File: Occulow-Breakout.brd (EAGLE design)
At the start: 49.5 x 50.8 mm, 18 parts

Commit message: Rearrangements and labeling
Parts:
- moved SL2 10.8 mm to (45.7, 23.2), turned to 270 degrees
- moved C1 3.81 mm to (47.5, 12.1)
- moved C2 3.81 mm to (44.3, 7.30)
- moved C3 3.81 mm to (43.8, 12.1)
- moved R4 3.81 mm to (45.9, 3.65)
- moved U$2 1.66 mm to (34.9, 14.4)
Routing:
- net GR_INT: track 25.1 -> 39.1 mm
- net GR_VCC: track 56.0 -> 43.7 mm
- net GR_SCL: track 26.5 -> 37.5 mm
- net GR_SDA: track 29.0 -> 38.8 mm
- net GR_GND: track 57.4 -> 48.1 mm
- net N$2: track 6.96 -> 9.66 mm
- net N$4: track 5.38 -> 6.77 mm
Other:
- board text added: "Grid-EYE Breakout"
- board text added: "INT"
- board text added: "PIR Breakout"
- board text added: "SCL"
- board text added: "SDA"

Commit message: Rename caps, bom
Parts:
- renumbered C10 to C4, C11 to C5
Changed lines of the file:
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@@
 <?xml version="1.0" encoding="utf-8"?>
 <!DOCTYPE eagle SYSTEM "eagle.dtd">
-<eagle version="8.0.0">
+<eagle version="8.0.2">
 <drawing>
 <settings>
@@
 <element name="U$3" library="SMA-JACK" package="SMA-JACK" value="SMA-JACKFEMALE" x="14.12875" y="45.72"/>
 <element name="U$4" library="PIR" package="IRS-B210ST01" value="IRS-B210ST01" x="31.4325" y="47.46625"/>
-<element name="C10" library="rcl" package="C1206" value="100uF" x="39.6875" y="47.3075" rot="R270"/>
+<element name="C4" library="rcl" package="C1206" value="100uF" x="39.6875" y="47.3075" rot="R270"/>
 <element name="R5" library="resistor" package="R1206" value="619k" x="36.67125" y="47.3075" rot="R270"/>
-<element name="C11" library="rcl" package="C1206" value="10uF" x="4.28625" y="3.81" rot="R270"/>
+<element name="C5" library="rcl" package="C1206" value="10uF" x="4.28625" y="3.81" rot="R270"/>
 <element name="SL1" library="con-amp-quick" package="03P" value="" x="35.40125" y="40.005" rot="R270">
 <attribute name="MF" value="" x="35.40125" y="40.005" size="1.778" layer="27" rot="R270" display="off"/>
+<attribute name="MPN" value="" x="35.40125" y="40.005" size="1.778" layer="27" rot="R270" display="off"/>
 <attribute name="OC_FARNELL" value="unknown" x="35.40125" y="40.005" size="1.778" layer="27" rot="R270" display="off"/>
 <attribute name="OC_NEWARK" value="unknown" x="35.40125" y="40.005" size="1.778" layer="27" rot="R270" display="off"/>
-<attribute name="MPN" value="" x="35.40125" y="40.005" size="1.778" layer="27" rot="R270" display="off"/>
 </element>
 <element name="SL2" library="con-amp-quick" package="05P" value="" x="45.72" y="23.1775" rot="R270">
 <attribute name="MF" value="" x="45.72" y="23.1775" size="1.778" layer="27" rot="R270" display="off"/>
+<attribute name="MPN" value="" x="45.72" y="23.1775" size="1.778" layer="27" rot="R270" display="off"/>
 <attribute name="OC_FARNELL" value="unknown" x="45.72" y="23.1775" size="1.778" layer="27" rot="R270" display="off"/>
 <attribute name="OC_NEWARK" value="unknown" x="45.72" y="23.1775" size="1.778" layer="27" rot="R270" display="off"/>
-<attribute name="MPN" value="" x="45.72" y="23.1775" size="1.778" layer="27" rot="R270" display="off"/>
 </element>
 <element name="SL3" library="con-amp-quick" package="07P" value="" x="15.39875" y="3.81" rot="R180">
 <attribute name="MF" value="" x="15.39875" y="3.81" size="1.778" layer="27" rot="R180" display="off"/>
+<attribute name="MPN" value="" x="15.39875" y="3.81" size="1.778" layer="27" rot="R180" display="off"/>
 <attribute name="OC_FARNELL" value="unknown" x="15.39875" y="3.81" size="1.778" layer="27" rot="R180" display="off"/>
 <attribute name="OC_NEWARK" value="unknown" x="15.39875" y="3.81" size="1.778" layer="27" rot="R180" display="off"/>
-<attribute name="MPN" value="" x="15.39875" y="3.81" size="1.778" layer="27" rot="R180" display="off"/>
 </element>
 </elements>
@@
 <signal name="N$5">
 <contactref element="U$4" pad="3"/>
-<contactref element="C10" pad="1"/>
+<contactref element="C4" pad="1"/>
 <contactref element="R5" pad="1"/>
 <wire x1="33.5825" y1="48.19125" x2="36.133" y2="48.19125" width="0.4064" layer="1"/>
@@
 <contactref element="U$1" pad="12"/>
 <contactref element="U$1" pad="34"/>
-<contactref element="C11" pad="1"/>
+<contactref element="C5" pad="1"/>
 <contactref element="SL3" pad="7"/>
 <wire x1="21.74875" y1="27.94" x2="20.47875" y2="27.94" width="0.4064" layer="1"/>
@@
 <contactref element="U$4" pad="5"/>
 <contactref element="U$4" pad="2"/>
-<contactref element="C10" pad="2"/>
+<contactref element="C4" pad="2"/>
 <contactref element="SL1" pad="3"/>
 <wire x1="29.2825" y1="46.01625" x2="29.2825" y2="48.91625" width="0.254" layer="1"/>
@@
 <contactref element="U$1" pad="41"/>
 <contactref element="U$1" pad="47"/>
-<contactref element="C11" pad="2"/>
+<contactref element="C5" pad="2"/>
 <contactref element="U$1" pad="20"/>
 <contactref element="U$1" pad="11"/>

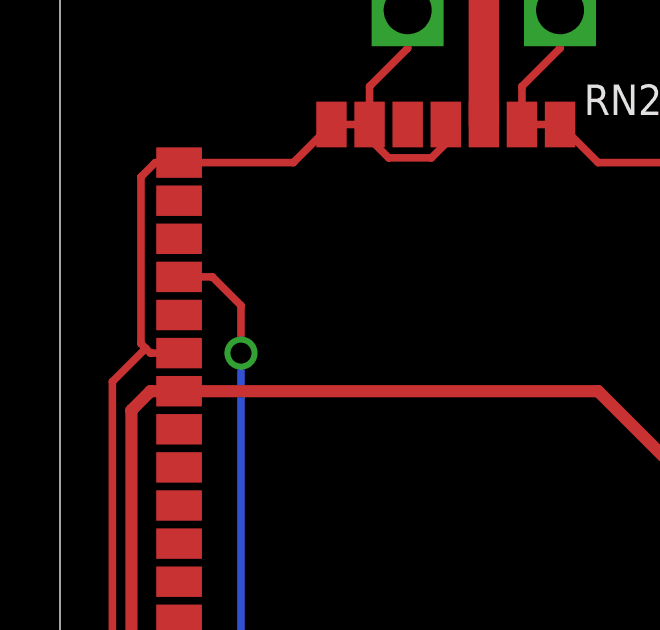
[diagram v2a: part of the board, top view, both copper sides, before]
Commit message: Correct reset for lora
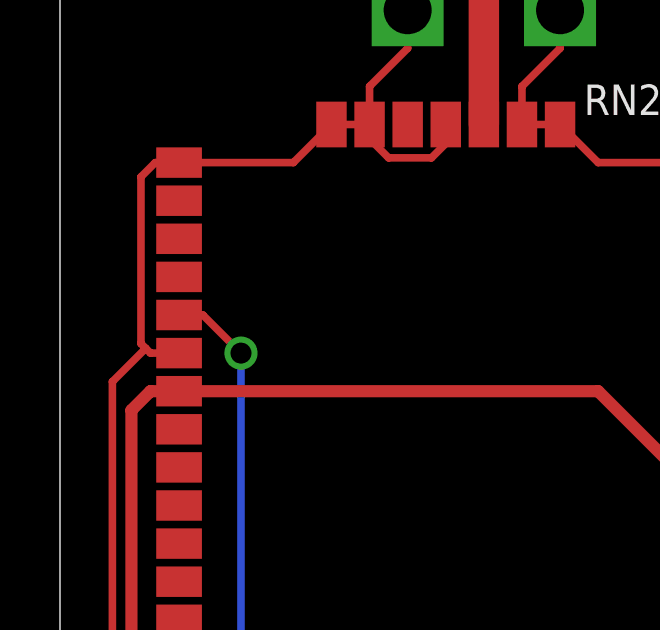
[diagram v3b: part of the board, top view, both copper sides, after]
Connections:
- net LR_RST_N: now also U$1.32; no longer U$1.31
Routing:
- net LR_RST_N: track 34.8 -> 33.4 mm
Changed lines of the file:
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@@
 </signal>
 <signal name="LR_RST_N">
-<contactref element="U$1" pad="31"/>
 <contactref element="SL3" pad="5"/>
-<wire x1="3.96875" y1="34.29" x2="5.08" y2="34.29" width="0.254" layer="1"/>
-<wire x1="5.08" y1="34.29" x2="6.0325" y2="33.3375" width="0.254" layer="1"/>
-<wire x1="6.0325" y1="33.3375" x2="6.0325" y2="31.75" width="0.254" layer="1"/>
 <via x="6.0325" y="31.75" extent="1-16" drill="0.7"/>
 <wire x1="6.0325" y1="31.75" x2="6.0325" y2="10.63625" width="0.254" layer="16"/>
 <wire x1="6.0325" y1="10.63625" x2="12.85875" y2="3.81" width="0.254" layer="16"/>
+<contactref element="U$1" pad="32"/>
+<wire x1="3.96875" y1="33.02" x2="4.7625" y2="33.02" width="0.254" layer="1"/>
+<wire x1="4.7625" y1="33.02" x2="6.0325" y2="31.75" width="0.254" layer="1"/>
 </signal>
 <signal name="PIR_GND">

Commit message: Added tplace layer for grideye
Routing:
- net PIR_GND: track 25.8 -> 33.3 mm
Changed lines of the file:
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@@
 <text x="40.005" y="36.67125" size="1.4224" layer="21" rot="R90">Occulow</text>
 <text x="41.11625" y="37.94125" size="0.6096" layer="21" rot="R90">PIR Breakout</text>
+<wire x1="30.32125" y1="50.165" x2="32.54375" y2="50.165" width="0.254" layer="21"/>
+<wire x1="30.48" y1="44.7675" x2="32.54375" y2="44.7675" width="0.254" layer="21"/>
 </plain>
 <attributes>
@@
 <contactref element="C4" pad="2"/>
 <contactref element="SL1" pad="3"/>
-<wire x1="29.2825" y1="46.01625" x2="29.2825" y2="48.91625" width="0.254" layer="1"/>
-<wire x1="29.2825" y1="48.91625" x2="31.09375" y2="48.91625" width="0.254" layer="1"/>
-<wire x1="31.09375" y1="48.91625" x2="32.54375" y2="47.46625" width="0.254" layer="1"/>
-<wire x1="32.54375" y1="47.46625" x2="33.5825" y2="47.46625" width="0.254" layer="1"/>
+<wire x1="29.2825" y1="48.91625" x2="29.2825" y2="46.01625" width="0.254" layer="1"/>
 <wire x1="39.6875" y1="45.9075" x2="39.6875" y2="40.005" width="0.254" layer="1"/>
 <wire x1="39.6875" y1="40.005" x2="37.1475" y2="37.465" width="0.254" layer="1"/>
-<wire x1="37.1475" y1="37.465" x2="35.40125" y2="37.465" width="0.254" layer="1"/>
+<wire x1="35.40125" y1="37.465" x2="37.1475" y2="37.465" width="0.254" layer="1"/>
 <wire x1="33.5825" y1="47.46625" x2="38.12875" y2="47.46625" width="0.254" layer="1"/>
 <wire x1="38.12875" y1="47.46625" x2="39.6875" y2="45.9075" width="0.254" layer="1"/>
+<wire x1="29.2825" y1="46.01625" x2="29.2825" y2="41.36125" width="0.254" layer="1"/>
+<wire x1="29.2825" y1="41.36125" x2="33.17875" y2="37.465" width="0.254" layer="1"/>
+<wire x1="33.17875" y1="37.465" x2="35.40125" y2="37.465" width="0.254" layer="1"/>
 </signal>
 <signal name="LR_GND">

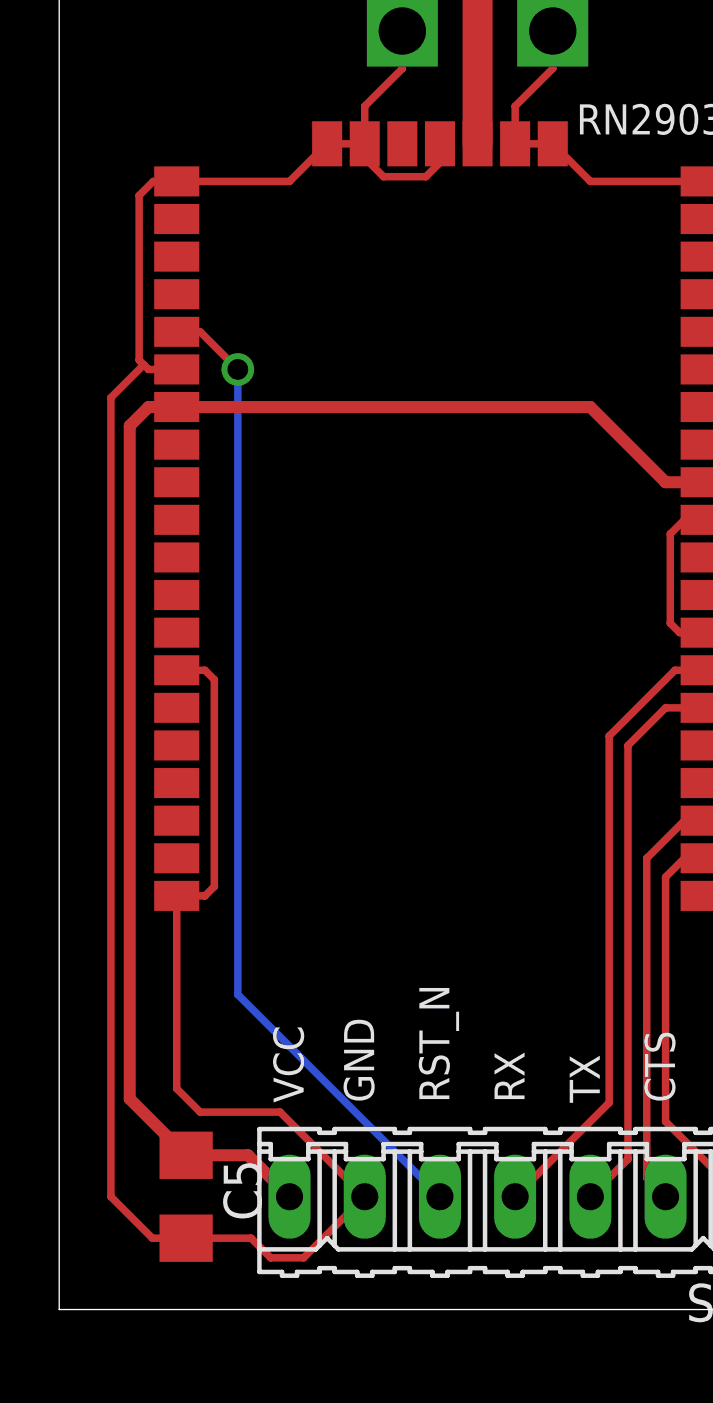
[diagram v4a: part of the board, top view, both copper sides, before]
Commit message: Re-route reset, no vias
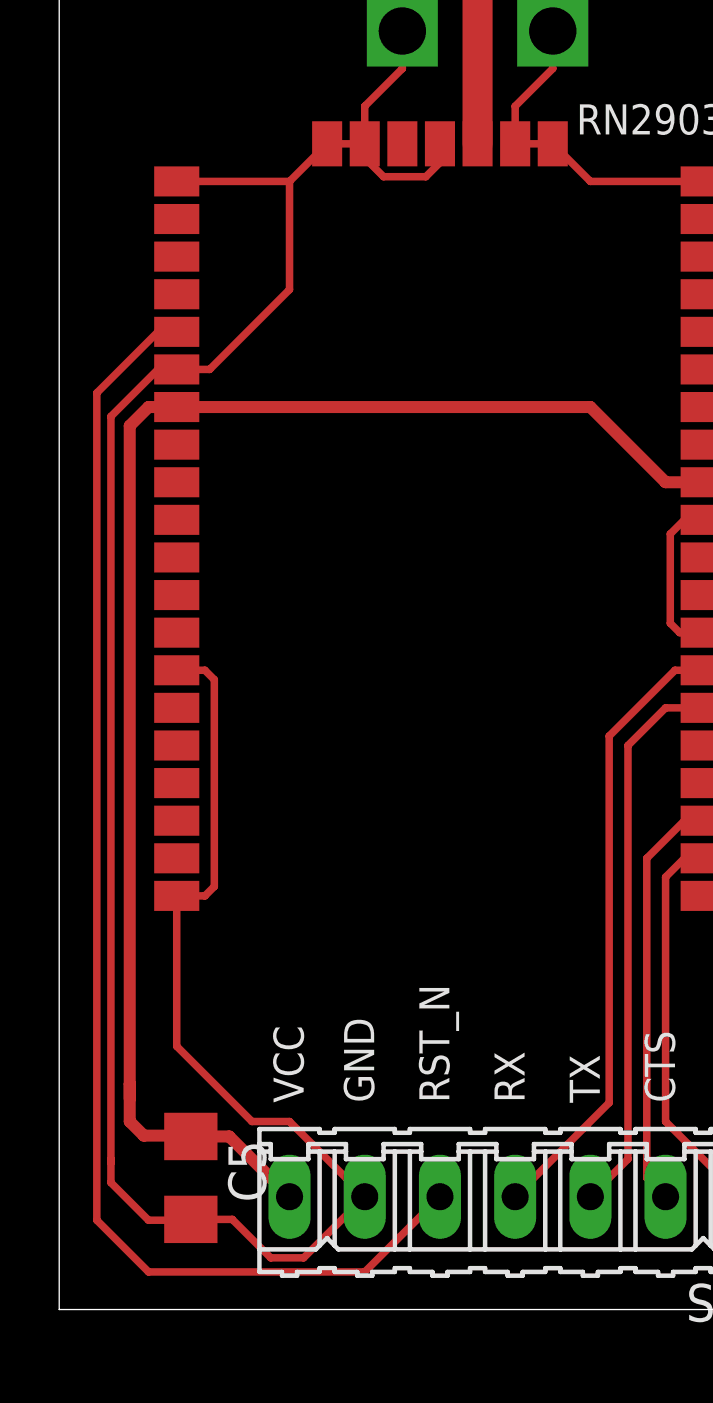
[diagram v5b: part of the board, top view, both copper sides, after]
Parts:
- moved C5 0.65 mm to (4.45, 4.45)
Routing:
- net LR_RST_N: track 33.4 -> 44.9 mm, vias 1 -> 0
- net LR_VCC: track 50.2 -> 51.1 mm
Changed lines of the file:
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@@
 <element name="C4" library="rcl" package="C1206" value="100uF" x="39.6875" y="47.3075" rot="R270"/>
 <element name="R5" library="resistor" package="R1206" value="619k" x="36.67125" y="47.3075" rot="R270"/>
-<element name="C5" library="rcl" package="C1206" value="10uF" x="4.28625" y="3.81" rot="R270"/>
+<element name="C5" library="rcl" package="C1206" value="10uF" x="4.445" y="4.445" rot="R270"/>
 <element name="SL1" library="con-amp-quick" package="03P" value="" x="35.40125" y="40.005" rot="R270">
 <attribute name="MF" value="" x="35.40125" y="40.005" size="1.778" layer="27" rot="R270" display="off"/>
@@
 <wire x1="3.96875" y1="30.48" x2="3.01625" y2="30.48" width="0.4064" layer="1"/>
 <wire x1="3.01625" y1="30.48" x2="2.38125" y2="29.845" width="0.4064" layer="1"/>
-<wire x1="2.38125" y1="29.845" x2="2.38125" y2="7.115" width="0.4064" layer="1"/>
-<wire x1="2.38125" y1="7.115" x2="4.28625" y2="5.21" width="0.4064" layer="1"/>
-<wire x1="4.28625" y1="5.21" x2="6.37875" y2="5.21" width="0.4064" layer="1"/>
-<wire x1="6.37875" y1="5.21" x2="7.77875" y2="3.81" width="0.4064" layer="1"/>
+<wire x1="2.38125" y1="29.845" x2="2.38125" y2="7.62" width="0.4064" layer="1"/>
+<wire x1="2.38125" y1="7.62" x2="2.38125" y2="7.115" width="0.4064" layer="1"/>
+<wire x1="2.38125" y1="7.62" x2="2.38125" y2="6.35" width="0.4064" layer="1"/>
+<wire x1="2.38125" y1="6.35" x2="2.8575" y2="5.87375" width="0.4064" layer="1"/>
+<wire x1="2.8575" y1="5.87375" x2="4.41625" y2="5.87375" width="0.4064" layer="1"/>
+<wire x1="4.41625" y1="5.87375" x2="4.445" y2="5.845" width="0.4064" layer="1"/>
+<wire x1="4.445" y1="5.845" x2="5.74375" y2="5.845" width="0.4064" layer="1"/>
+<wire x1="5.74375" y1="5.845" x2="7.77875" y2="3.81" width="0.4064" layer="1"/>
 </signal>
 <signal name="LR_RST_N">
 <contactref element="SL3" pad="5"/>
-<via x="6.0325" y="31.75" extent="1-16" drill="0.7"/>
-<wire x1="6.0325" y1="31.75" x2="6.0325" y2="10.63625" width="0.254" layer="16"/>
-<wire x1="6.0325" y1="10.63625" x2="12.85875" y2="3.81" width="0.254" layer="16"/>
 <contactref element="U$1" pad="32"/>
-<wire x1="3.96875" y1="33.02" x2="4.7625" y2="33.02" width="0.254" layer="1"/>
-<wire x1="4.7625" y1="33.02" x2="6.0325" y2="31.75" width="0.254" layer="1"/>
+<wire x1="3.96875" y1="33.02" x2="3.33375" y2="33.02" width="0.254" layer="1"/>
+<wire x1="3.33375" y1="33.02" x2="1.27" y2="30.95625" width="0.254" layer="1"/>
+<wire x1="1.27" y1="30.95625" x2="1.27" y2="3.01625" width="0.254" layer="1"/>
+<wire x1="1.27" y1="3.01625" x2="3.01625" y2="1.27" width="0.254" layer="1"/>
+<wire x1="3.01625" y1="1.27" x2="10.31875" y2="1.27" width="0.254" layer="1"/>
+<wire x1="10.31875" y1="1.27" x2="12.85875" y2="3.81" width="0.254" layer="1"/>
 </signal>
 <signal name="PIR_GND">
@@
 <wire x1="23.01875" y1="22.38375" x2="23.01875" y2="14.2875" width="0.254" layer="1"/>
 <contactref element="SL3" pad="6"/>
-<wire x1="4.7625" y1="6.6675" x2="3.96875" y2="7.46125" width="0.254" layer="1"/>
-<wire x1="4.7625" y1="6.6675" x2="7.46125" y2="6.6675" width="0.254" layer="1"/>
-<wire x1="10.31875" y1="3.81" x2="7.46125" y2="6.6675" width="0.254" layer="1"/>
-<wire x1="6.48" y1="2.41" x2="7.14375" y2="1.74625" width="0.254" layer="1"/>
 <wire x1="7.14375" y1="1.74625" x2="8.255" y2="1.74625" width="0.254" layer="1"/>
-<wire x1="8.255" y1="1.74625" x2="10.31875" y2="3.81" width="0.254" layer="1"/>
+<wire x1="10.31875" y1="3.81" x2="8.255" y2="1.74625" width="0.254" layer="1"/>
 <contactref element="U$3" pad="1"/>
 <contactref element="U$3" pad="2"/>
@@
 <wire x1="17.93875" y1="38.1" x2="16.66875" y2="39.37" width="0.254" layer="1"/>
 <wire x1="9.04875" y1="39.37" x2="7.77875" y2="38.1" width="0.254" layer="1"/>
-<wire x1="6.48" y1="2.41" x2="4.28625" y2="2.41" width="0.254" layer="1"/>
-<wire x1="3.96875" y1="13.97" x2="3.96875" y2="7.46125" width="0.254" layer="1"/>
 <wire x1="21.74875" y1="38.1" x2="17.93875" y2="38.1" width="0.254" layer="1"/>
 <wire x1="7.77875" y1="38.1" x2="3.96875" y2="38.1" width="0.254" layer="1"/>
 <wire x1="10.31875" y1="40.64" x2="10.31875" y2="39.37" width="0.254" layer="1"/>
 <wire x1="15.39875" y1="40.64" x2="15.39875" y2="39.37" width="0.254" layer="1"/>
-<wire x1="3.96875" y1="38.1" x2="3.175" y2="38.1" width="0.254" layer="1"/>
-<wire x1="3.175" y1="38.1" x2="2.69875" y2="37.62375" width="0.254" layer="1"/>
-<wire x1="2.69875" y1="37.62375" x2="2.69875" y2="32.0675" width="0.254" layer="1"/>
-<wire x1="2.8575" y1="31.90875" x2="2.69875" y2="32.0675" width="0.254" layer="1"/>
-<wire x1="2.8575" y1="31.90875" x2="3.01625" y2="31.75" width="0.254" layer="1"/>
-<wire x1="3.01625" y1="31.75" x2="3.96875" y2="31.75" width="0.254" layer="1"/>
-<wire x1="4.28625" y1="2.41" x2="3.14625" y2="2.41" width="0.254" layer="1"/>
-<wire x1="3.14625" y1="2.41" x2="1.74625" y2="3.81" width="0.254" layer="1"/>
-<wire x1="1.74625" y1="3.81" x2="1.74625" y2="30.7975" width="0.254" layer="1"/>
-<wire x1="1.74625" y1="30.7975" x2="2.8575" y2="31.90875" width="0.254" layer="1"/>
 <wire x1="3.96875" y1="21.59" x2="4.92125" y2="21.59" width="0.254" layer="1"/>
 <wire x1="4.92125" y1="21.59" x2="5.23875" y2="21.2725" width="0.254" layer="1"/>
@@
 <wire x1="5.23875" y1="14.2875" x2="4.92125" y2="13.97" width="0.254" layer="1"/>
 <wire x1="4.92125" y1="13.97" x2="3.96875" y2="13.97" width="0.254" layer="1"/>
+<wire x1="7.77875" y1="38.1" x2="7.77875" y2="34.44875" width="0.254" layer="1"/>
+<wire x1="7.77875" y1="34.44875" x2="5.08" y2="31.75" width="0.254" layer="1"/>
+<wire x1="5.08" y1="31.75" x2="3.96875" y2="31.75" width="0.254" layer="1"/>
+<wire x1="3.96875" y1="31.75" x2="3.33375" y2="31.75" width="0.254" layer="1"/>
+<wire x1="3.33375" y1="31.75" x2="1.74625" y2="30.1625" width="0.254" layer="1"/>
+<wire x1="1.74625" y1="30.1625" x2="1.74625" y2="5.08" width="0.254" layer="1"/>
+<wire x1="1.74625" y1="5.08" x2="1.74625" y2="4.95" width="0.254" layer="1"/>
+<wire x1="1.74625" y1="5.08" x2="1.74625" y2="4.28625" width="0.254" layer="1"/>
+<wire x1="1.74625" y1="4.28625" x2="3.01625" y2="3.01625" width="0.254" layer="1"/>
+<wire x1="3.01625" y1="3.01625" x2="4.41625" y2="3.01625" width="0.254" layer="1"/>
+<wire x1="4.41625" y1="3.01625" x2="4.445" y2="3.045" width="0.254" layer="1"/>
+<wire x1="4.445" y1="3.045" x2="5.845" y2="3.045" width="0.254" layer="1"/>
+<wire x1="5.845" y1="3.045" x2="7.14375" y2="1.74625" width="0.254" layer="1"/>
+<wire x1="3.96875" y1="13.97" x2="3.96875" y2="8.89" width="0.254" layer="1"/>
+<wire x1="3.96875" y1="8.89" x2="6.50875" y2="6.35" width="0.254" layer="1"/>
+<wire x1="6.50875" y1="6.35" x2="7.77875" y2="6.35" width="0.254" layer="1"/>
+<wire x1="7.77875" y1="6.35" x2="10.31875" y2="3.81" width="0.254" layer="1"/>
 </signal>
 <signal name="GR_GND">
